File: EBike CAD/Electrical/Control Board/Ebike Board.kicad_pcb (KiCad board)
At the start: 2 copper layers, 51.7 x 87.6 mm, 32 parts, among them J1 Conn_01x02_Female, J10 Conn_01x05_Female, J11 Conn_01x05_Female, J2 Conn_01x05_Female, J3 Conn_01x04_Female, J4 Conn_01x02_Female, J5 Conn_01x03_Female, J6 Conn_01x04_Female, J7 USB_B_Micro, J8 Conn_01x05_Female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

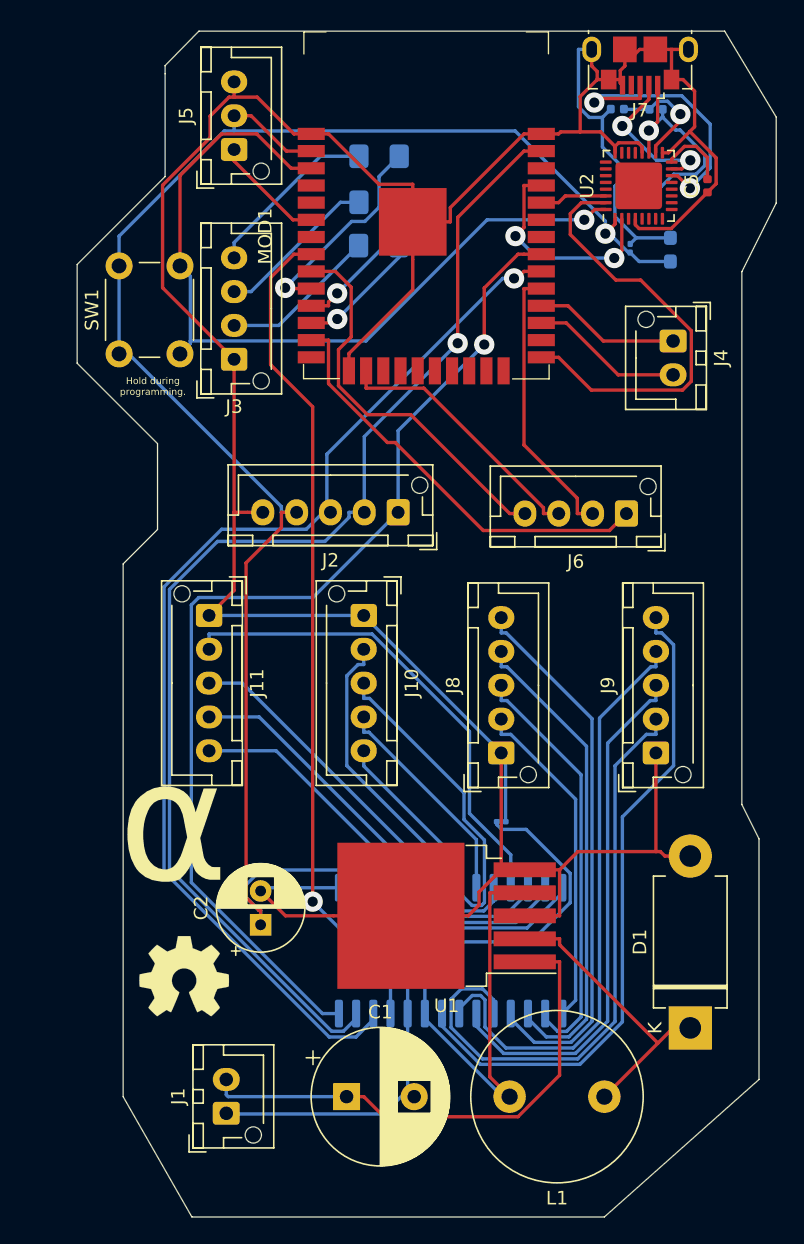
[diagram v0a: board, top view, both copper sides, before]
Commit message: -Software ported to new ESP32 board -Added OTA updates -Added bluetooth serial debug -Added IOexpander -Added headlight functionality
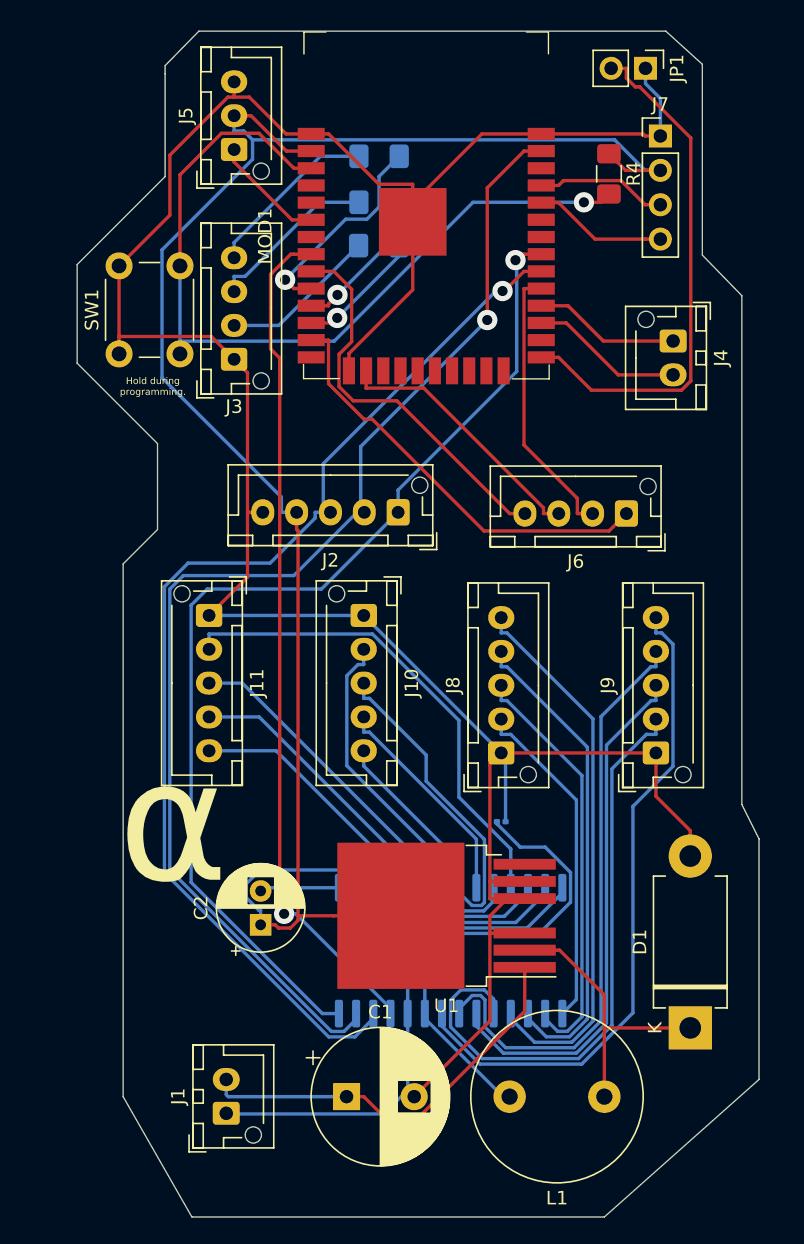
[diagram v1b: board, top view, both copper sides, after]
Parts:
- removed C3, C6: 4.7uF, Resistor_SMD:R_0603_1608Metric_Pad1.05x0.95mm_HandSolder
- removed C4, C7: 0.1uF, Resistor_SMD:R_0201_0603Metric
- removed C5: 1uF, Resistor_SMD:R_0402_1005Metric
- removed R5: 10k, Resistor_SMD:R_0402_1005Metric
- removed REF**: OSHW-Symbol_6.7x6mm_SilkScreen, Symbol:OSHW-Symbol_6.7x6mm_SilkScreen
- removed U2: CY7C65213A-32LTXI, Package_DFN_QFN:QFN-32-1EP_5x5mm_P0.5mm_EP3.45x3.45mm
- added JP1: Jumper_NO_Small, Connector_PinHeader_2.54mm:PinHeader_1x02_P2.54mm_Vertical, F.Cu at (152.9, 72.6)
- J7: value USB_B_Micro -> 0022232041; footprint Connector_USB:USB_Micro-B_GCT_USB3076-30-A -> Connector_PinHeader_2.54mm:PinHeader_1x04_P2.54mm_Vertical
- R4: value 4.7k -> 10k; footprint Resistor_SMD:R_0402_1005Metric -> Resistor_SMD:R_1206_3216Metric_Pad1.42x1.75mm_HandSolder; moved to F.Cu
- U1: footprint Package_TO_SOT_SMD:TO-263-5_TabPin6 -> Package_TO_SOT_SMD:TO-263-6
- moved R4 5.91 mm to (150.2, 80.4), turned to 270 degrees
- moved J7 5.41 mm to (154.0, 77.6), turned to 0 degrees
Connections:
- J7 pad 1: /USB/VBUS -> GND
- J7 pad 2: Net-(J7-Pad2) -> 3v3
- J7 pad 3: Net-(J7-Pad3) -> /ESP32/TXD
- J7 pad 4: Net-(J7-Pad4) -> /ESP32/RXD
- MOD1 pad 25: DTR -> /ESP32/BOOT
- MOD1 pad 3: RTS -> Net-(MOD1-Pad3)
- MOD1 pad 34: RXD -> /ESP32/RXD
- MOD1 pad 35: TXD -> /ESP32/TXD
- R4 pad 1: /USB/VBUS -> 3v3
- R4 pad 2: Net-(R4-Pad2) -> Net-(MOD1-Pad3)
- SW1 pad 1: 3v3 -> GND
- SW1 pad 2: RTS -> Net-(MOD1-Pad3)
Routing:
- net Net-(MOD1-Pad3): track 0.00 -> 61.5 mm, vias 0 -> 1
- net RTS: track 60.6 -> 0.00 mm, vias 1 -> 0
- net GND: track 291.0 -> 239.0 mm
- net /ESP32/BOOT: track 0.00 -> 38.7 mm
- net DTR: track 32.5 -> 0.00 mm
- net Net-(J7-Pad3): track 21.2 -> 0.00 mm, vias 2 -> 0
- net /USB/VBUS: track 19.0 -> 0.00 mm, vias 1 -> 0
- net TXD: track 16.4 -> 0.00 mm, vias 2 -> 0
- net 3v3: track 192.2 -> 176.9 mm, vias 1 -> 0
- net Net-(J7-Pad2): track 11.5 -> 0.00 mm, vias 2 -> 0
- net /ESP32/RXD: track 0.00 -> 9.92 mm
- net /ESP32/TXD: track 0.00 -> 9.69 mm
- net /Power/VBat: track 38.7 -> 30.2 mm
- net Net-(R4-Pad2): track 8.44 -> 0.00 mm, vias 1 -> 0
- net Net-(C5-Pad2): track 5.20 -> 0.00 mm
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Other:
- board size 51.7 x 87.6 mm -> 50.4 x 87.6 mm
- board text added: "Ebike Controller V2.2"
- board text removed: "Ebike Controller V2.1"

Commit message: some hacks to fix broken uart and replace it with ppm
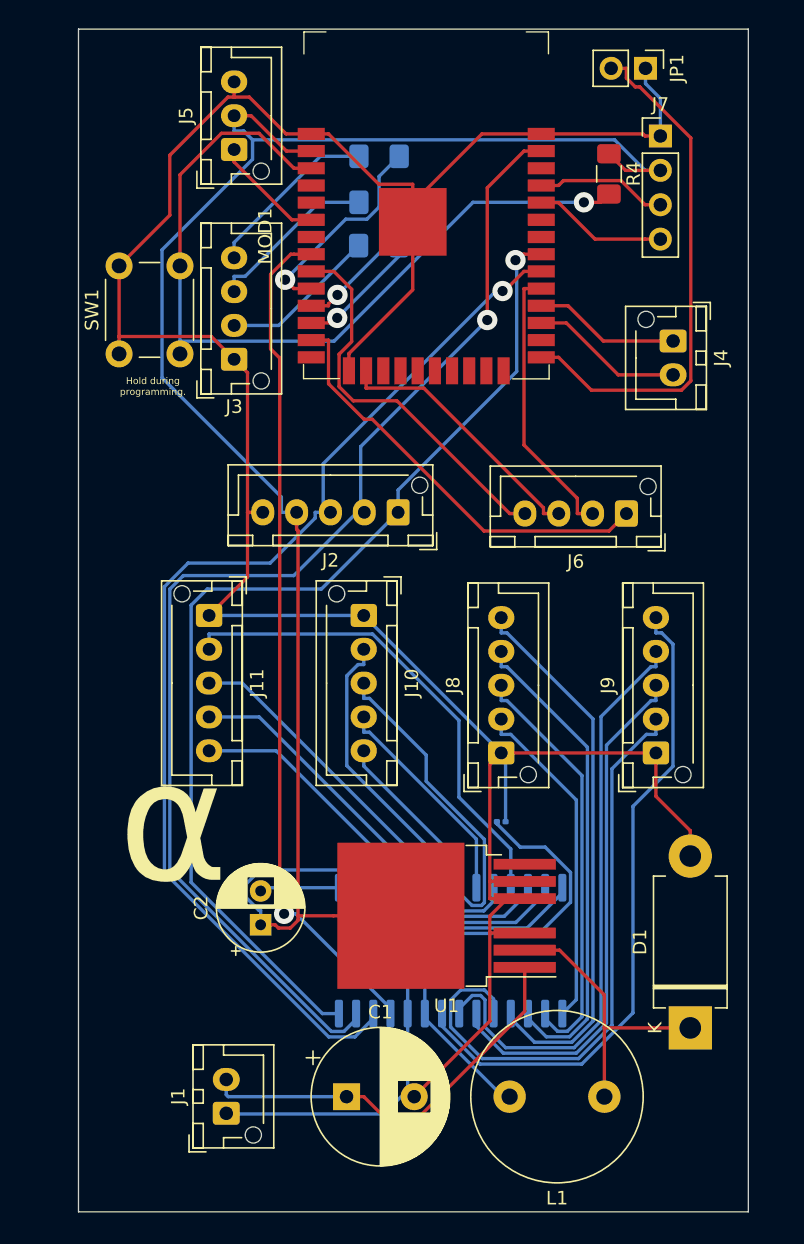
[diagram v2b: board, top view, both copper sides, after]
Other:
- board size 50.4 x 87.6 mm -> 49.5 x 87.4 mm

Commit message: new hw revision
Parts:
- added J12: Conn_01x04_Female, Connector_JST:JST_XH_B4B-XH-AM_1x04_P2.50mm_Vertical, F.Cu at (115.4, 100.4)
- moved SW1 7.41 mm to (113.7, 86.3)
- moved J7 5.32 mm to (159.0, 79.4)
- moved JP1 2.02 mm to (151.4, 71.2)
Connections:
- MOD1 pad 33: Net-(MOD1-Pad33) -> SDA
- MOD1 pad 36: Net-(MOD1-Pad36) -> SCL
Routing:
- net GND: track 239.0 -> 0.00 mm
- net 3v3: track 176.9 -> 0.00 mm
- net MOSI: track 89.9 -> 0.00 mm, vias 1 -> 0
- net SCK: track 82.9 -> 0.00 mm, vias 1 -> 0
- net MISO: track 77.9 -> 0.00 mm, vias 1 -> 0
- net IOExpanderCS: track 62.4 -> 0.00 mm, vias 1 -> 0
- net Net-(MOD1-Pad3): track 61.5 -> 0.00 mm, vias 1 -> 0
- net Net-(J9-Pad5): track 49.0 -> 0.00 mm
- net Net-(J9-Pad2): track 45.1 -> 0.00 mm
- net Net-(J9-Pad4): track 44.0 -> 0.00 mm
- net Net-(J8-Pad5): track 40.7 -> 0.00 mm
- net Net-(J9-Pad3): track 39.0 -> 0.00 mm
- net /ESP32/BOOT: track 38.7 -> 0.00 mm
- net Net-(J11-Pad2): track 36.2 -> 0.00 mm
- net Net-(J8-Pad4): track 35.9 -> 0.00 mm
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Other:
- board text added: "Ebike Controller V2.3"
- board text added: "Klayton Smith 7/11/2020"
- board text added: "β"
- board text removed: "Ebike Controller V2.2"
- board text removed: "Hold during programming."
- board text removed: "Klayton Smith 4/12/2020"
- board text removed: "α"

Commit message: routed pcb
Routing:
- net GND: track 0.00 -> 255.2 mm
- net 3v3: track 0.00 -> 199.2 mm
- net MISO: track 0.00 -> 104.9 mm
- net MOSI: track 0.00 -> 90.3 mm, vias 0 -> 1
- net SCK: track 0.00 -> 86.7 mm
- net IOExpanderCS: track 0.00 -> 61.8 mm, vias 0 -> 1
- net Net-(MOD1-Pad3): track 0.00 -> 53.9 mm, vias 0 -> 1
- net /ESP32/ExtraCS3: track 0.00 -> 52.7 mm
- net Net-(J9-Pad5): track 0.00 -> 47.9 mm
- net Net-(J9-Pad4): track 0.00 -> 46.3 mm
- net Net-(J8-Pad5): track 0.00 -> 40.7 mm
- net Net-(J9-Pad3): track 0.00 -> 40.5 mm
- net SCL: track 0.00 -> 37.5 mm, vias 0 -> 1
- net /ESP32/BOOT: track 0.00 -> 37.4 mm, vias 0 -> 1
- net SDA: track 0.00 -> 37.1 mm, vias 0 -> 1
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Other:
- board text added: "Ebike Controller V2"
- board text removed: "Ebike Controller V2.3"

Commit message: fix
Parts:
- added mp1: MountingHole_3.2mm_M3, MountingHole:MountingHole_3.2mm_M3, F.Cu at (157.0, 153.6)
- added mp2: MountingHole_3.2mm_M3, MountingHole:MountingHole_3.2mm_M3, F.Cu at (114.5, 153.6)
- added mp3: MountingHole_3.2mm_M3, MountingHole:MountingHole_3.2mm_M3, F.Cu at (114.5, 73.2)
- added mp4: MountingHole_3.2mm_M3, MountingHole:MountingHole_3.2mm_M3, F.Cu at (157.0, 73.2)
- U1: footprint Package_TO_SOT_SMD:TO-263-6 -> Package_TO_SOT_SMD:TO-263-5_TabPin6
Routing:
- net /ESP32/NFC_CS: track 28.7 -> 106.2 mm, vias 1 -> 0
- net IOExpanderCS: track 61.8 -> 101.5 mm
- net /ESP32/ExtraCS3: track 52.7 -> 26.2 mm, vias 0 -> 1
- net MISO: track 104.9 -> 80.9 mm, vias 0 -> 1
- net /ESP32/ExtraCS2: track 19.6 -> 31.7 mm
- net /ESP32/BOOT: track 37.4 -> 47.6 mm, vias 1 -> 0
- net GND: track 255.2 -> 264.4 mm
- net /ESP32/Throttle: track 26.7 -> 19.8 mm
- net 3v3: track 199.2 -> 204.2 mm
- net /Power/VBat: track 27.3 -> 32.1 mm
- net SCL: track 37.5 -> 41.7 mm, vias 1 -> 0
- net Net-(MOD1-Pad3): track 53.9 -> 51.4 mm
- net Net-(D1-Pad1): track 23.6 -> 21.6 mm
- net Net-(MOD1-Pad10): track 14.1 -> 15.7 mm
- net SCK: track 86.7 -> 85.3 mm
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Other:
- outline, holes or cut-outs redrawn
